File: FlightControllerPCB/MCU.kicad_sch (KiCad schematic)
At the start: 1 part, among them U5 STM32F745VGTx

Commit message: Early MCU Setup
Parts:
- added C10, C11, C12, C7, C8, C9: .1uF, symbol Device:C
- added C6: 10uF, symbol Device:C
- added R10: 10k, symbol Device:R
- added SW3: SW_Push, symbol Switch:SW_Push
- added SW4: SW_SPDT, symbol Switch:SW_SPDT
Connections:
- net GND: now reaches U5.10 (VSS), U5.26 (VSS), U5.49 (VSS), U5.74 (VSS), U5.99 (VSS)
- net GND: now also U5.19 (VSSA), C10.2, C11.2, C12.2, C6.2, C7.1, C8.2, C9.2, SW3.1, SW4.1 (A)
- net +3.3V: now reaches U5.100 (VDD)
- net +3.3V: now also U5.11 (VDD), U5.27 (VDD), U5.50 (VDD), U5.6 (VBAT), U5.75 (VDD), C10.1, C11.1, C12.1, C6.1, C8.1, C9.1, SW4.3 (C)
- net at U5.14 (NRST): now also C7.2, SW3.2
- net SWDIO: now reaches U5.72 (PA13)
- net SWDCLK: now reaches U5.76 (PA14)
- net at U5.94 (BOOT0): now also R10.1
- new net: R10.2, SW4.2 (B)

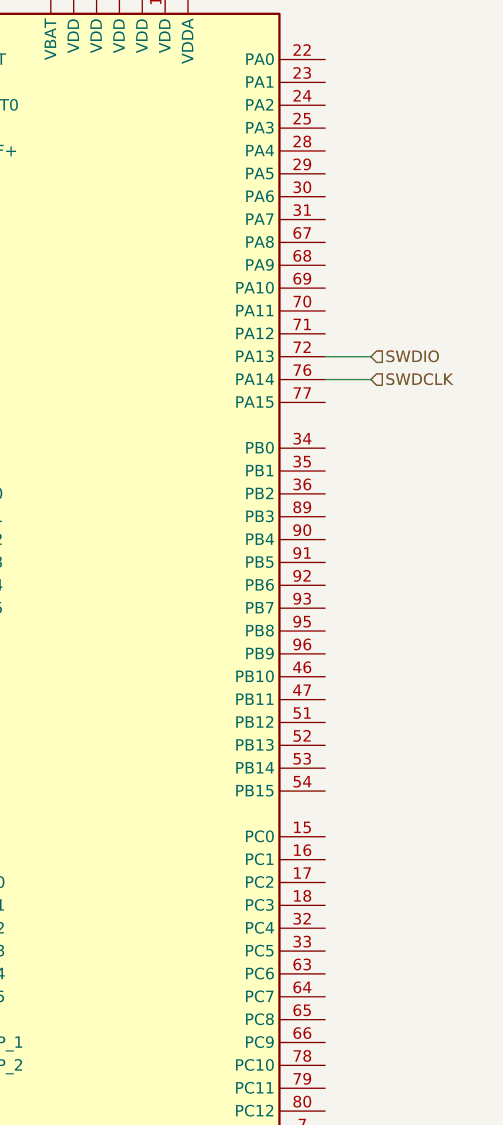
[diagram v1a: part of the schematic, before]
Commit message: initial baro/imu to mcu pins
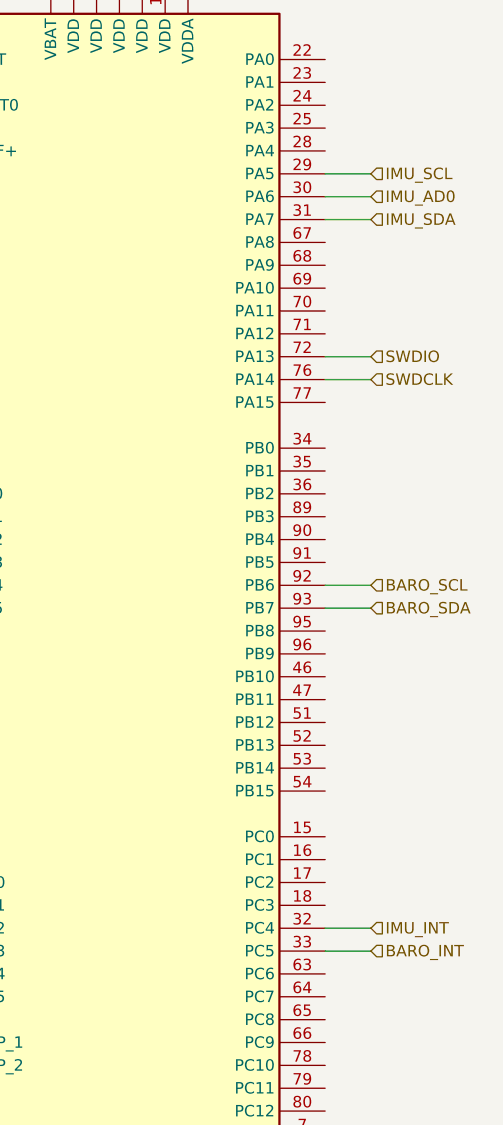
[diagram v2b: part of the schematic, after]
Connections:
- net IMU_SCL: now reaches U5.29 (PA5)
- net IMU_AD0: now reaches U5.30 (PA6)
- net IMU_SDA: now reaches U5.31 (PA7)
- net IMU_INT: now reaches U5.32 (PC4)
- net BARO_INT: now reaches U5.33 (PC5)
- net BARO_SCL: now reaches U5.92 (PB6)
- net BARO_SDA: now reaches U5.93 (PB7)
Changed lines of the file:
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@@
+	(wire
+		(pts
+			(xy 158.75 142.24) (xy 163.83 142.24)
+		)
+		(stroke
+			(width 0)
+			(type default)
+		)
+	)
 	(wire
 		(pts
@@
 	(wire
 		(pts
+			(xy 158.75 104.14) (xy 163.83 104.14)
+		)
+		(stroke
+			(width 0)
+			(type default)
+		)
+	)
+	(wire
+		(pts
 			(xy 93.98 20.32) (xy 104.14 20.32)
 		)
@@
 	(wire
 		(pts
+			(xy 158.75 139.7) (xy 163.83 139.7)
+		)
+		(stroke
+			(width 0)
+			(type default)
+		)
+	)
+	(wire
+		(pts
+			(xy 158.75 101.6) (xy 163.83 101.6)
+		)
+		(stroke
+			(width 0)
+			(type default)
+		)
+	)
+	(wire
+		(pts
+			(xy 158.75 55.88) (xy 163.83 55.88)
+		)
+		(stroke
+			(width 0)
+			(type default)
+		)
+	)
+	(wire
+		(pts
 			(xy 96.52 31.75) (xy 106.68 31.75)
 		)
@@
 	(wire
 		(pts
+			(xy 158.75 60.96) (xy 163.83 60.96)
+		)
+		(stroke
+			(width 0)
+			(type default)
+		)
+	)
+	(wire
+		(pts
 			(xy 83.82 20.32) (xy 93.98 20.32)
 		)
@@
 	(wire
 		(pts
+			(xy 158.75 58.42) (xy 163.83 58.42)
+		)
+		(stroke
+			(width 0)
+			(type default)
+		)
+	)
+	(wire
+		(pts
 			(xy 92.71 48.26) (xy 113.03 48.26)
 		)
@@
 		)
 	)
+	(hierarchical_label "IMU_SCL"
+		(shape input)
+		(at 163.83 55.88 0)
+		(effects
+			(font
+				(size 1.27 1.27)
+			)
+			(justify left)
+		)
+	)
+	(hierarchical_label "IMU_INT"
+		(shape input)
+		(at 163.83 139.7 0)
+		(effects
+			(font
+				(size 1.27 1.27)
+			)
+			(justify left)
+		)
+	)
+	(hierarchical_label "BARO_SDA"
+		(shape input)
+		(at 163.83 104.14 0)
+		(effects
+			(font
+				(size 1.27 1.27)
+			)
+			(justify left)
+		)
+	)
+	(hierarchical_label "BARO_SCL"
+		(shape input)
+		(at 163.83 101.6 0)
+		(effects
+			(font
+				(size 1.27 1.27)
+			)
+			(justify left)
+		)
+	)
 	(hierarchical_label "SWDCLK"
 		(shape input)
@@
 		)
 	)
+	(hierarchical_label "BARO_INT"
+		(shape input)
+		(at 163.83 142.24 0)
+		(effects
+			(font
+				(size 1.27 1.27)
+			)
+			(justify left)
+		)
+	)
+	(hierarchical_label "IMU_SDA"
+		(shape input)
+		(at 163.83 60.96 0)
+		(effects
+			(font
+				(size 1.27 1.27)
+			)
+			(justify left)
+		)
+	)
 	(hierarchical_label "SWDIO"
 		(shape input)
@@
 		(effects
 			(font
+				(size 1.27 1.27)
+			)
+			(justify left)
+		)
+	)
+	(hierarchical_label "IMU_AD0"
+		(shape input)
+		(at 163.83 58.42 0)
+		(effects
+			(font

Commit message: actually the IMU+baro changes
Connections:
- net IMU_FSYNC: now reaches U5.23 (PA1)
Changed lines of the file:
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@@
+	(wire
+		(pts
+			(xy 158.75 45.72) (xy 163.83 45.72)
+		)
+		(stroke
+			(width 0)
+			(type default)
+		)
+	)
 	(wire
 		(pts
@@
 		(effects
 			(font
+				(size 1.27 1.27)
+			)
+			(justify left)
+		)
+	)
+	(hierarchical_label "IMU_FSYNC"
+		(shape input)
+		(at 163.83 45.72 0)
+		(effects
+			(font

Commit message: Power circuit
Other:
- note added: "- Jeson connector (UART+JST) - USB(D+,D-) - 6 pin micro JST for GPS - extra header + resistors"
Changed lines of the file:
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@@
 	(generator_version "10.0")
 	(paper "A4")
+	(text "- Jeson connector (UART+JST)\n- USB(D+,D-)\n- 6 pin micro JST for GPS\n- extra header + resistors"
+		(exclude_from_sim no)
+		(at 219.456 45.974 0)
+		(effects
+			(font
+				(size 2.54 2.54)
+			)
+		)
+	)
 	(junction
 		(at 73.66 27.94)

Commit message: early MCU setup
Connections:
- net SBC RX: now reaches U5.46 (PB10)
- net SBC TX: now reaches U5.47 (PB11)
- net SBC CTS: now reaches U5.51 (PB12)
- net SBC RTS: now reaches U5.52 (PB13)
- net USB Data -: now reaches U5.70 (PA11)
- net USB Data +: now reaches U5.71 (PA12)
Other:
- note added: "- RC conn"
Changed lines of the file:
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@@
 	(generator_version "10.0")
 	(paper "A4")
+	(text "- RC conn"
+		(exclude_from_sim no)
+		(at 203.2 56.896 0)
+		(effects
+			(font
+				(size 2.54 2.54)
+			)
+		)
+	)
 	(text "- Jeson connector (UART+JST)\n- USB(D+,D-)\n- 6 pin micro JST for GPS\n- extra header + resistors"
 		(exclude_from_sim no)
@@
 	(wire
 		(pts
+			(xy 163.83 71.12) (xy 158.75 71.12)
+		)
+		(stroke
+			(width 0)
+			(type default)
+		)
+	)
+	(wire
+		(pts
 			(xy 123.19 20.32) (xy 128.27 20.32)
 		)
@@
 	(wire
 		(pts
+			(xy 163.83 114.3) (xy 158.75 114.3)
+		)
+		(stroke
+			(width 0)
+			(type default)
+		)
+	)
+	(wire
+		(pts
 			(xy 104.14 27.94) (xy 114.3 27.94)
 		)
@@
 	(wire
 		(pts
+			(xy 163.83 116.84) (xy 158.75 116.84)
+		)
+		(stroke
+			(width 0)
+			(type default)
+		)
+	)
+	(wire
+		(pts
 			(xy 138.43 33.02) (xy 140.97 33.02)
 		)
@@
 	(wire
 		(pts
+			(xy 163.83 119.38) (xy 158.75 119.38)
+		)
+		(stroke
+			(width 0)
+			(type default)
+		)
+	)
+	(wire
+		(pts
 			(xy 158.75 45.72) (xy 163.83 45.72)
 		)
@@
 	(wire
 		(pts
+			(xy 163.83 111.76) (xy 158.75 111.76)
+		)
+		(stroke
+			(width 0)
+			(type default)
+		)
+	)
+	(wire
+		(pts
 			(xy 93.98 20.32) (xy 104.14 20.32)
 		)
@@
 	(wire
 		(pts
+			(xy 163.83 73.66) (xy 158.75 73.66)
+		)
+		(stroke
+			(width 0)
+			(type default)
+		)
+	)
+	(wire
+		(pts
 			(xy 96.52 31.75) (xy 106.68 31.75)
 		)
@@
 		)
 	)
+	(hierarchical_label "USB Data +"
+		(shape input)
+		(at 163.83 73.66 0)
+		(effects
+			(font
+				(size 1.27 1.27)
+			)
+			(justify left)
+		)
+	)
 	(hierarchical_label "BARO_SCL"
 		(shape input)
@@
 		)
 	)
+	(hierarchical_label "USB Data -"
+		(shape input)
+		(at 163.83 71.12 0)
+		(effects
+			(font
+				(size 1.27 1.27)
+			)
+			(justify left)
+		)
+	)
 	(hierarchical_label "BARO_INT"
 		(shape input)
@@
 		)
 	)
+	(hierarchical_label "SBC RTS"
+		(shape input)
+		(at 163.83 119.38 0)
+		(effects
+			(font
+				(size 1.27 1.27)
+			)
+			(justify left)
+		)
+	)
+	(hierarchical_label "SBC TX"
+		(shape input)
+		(at 163.83 114.3 0)
+		(effects
+			(font
+				(size 1.27 1.27)
+			)
+			(justify left)
+		)
+	)
 	(hierarchical_label "IMU_FSYNC"
 		(shape input)
@@
 		(effects
 			(font
+				(size 1.27 1.27)
+			)
+			(justify left)
+		)
+	)
+	(hierarchical_label "SBC RX"
+		(shape input)
+		(at 163.83 111.76 0)
+		(effects
+			(font
+				(size 1.27 1.27)
+			)
+			(justify left)
+		)
+	)
+	(hierarchical_label "SBC CTS"
+		(shape input)
+		(at 163.83 116.84 0)
+		(effects
+			(font
